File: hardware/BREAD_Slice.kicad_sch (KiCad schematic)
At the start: 23 parts, among them J1 I2C_01x04, J2 Conn_01x10_Female, J3 Screw_Terminal_01x02, J4 Screw_Terminal_01x02, J5 Screw_Terminal_01x02, J6 Screw_Terminal_01x02, U2 ACS723xMATR-10AB, U3 ACS723xMATR-10AB, U4 ACS723xMATR-10AB, U5 ACS723xMATR-10AB

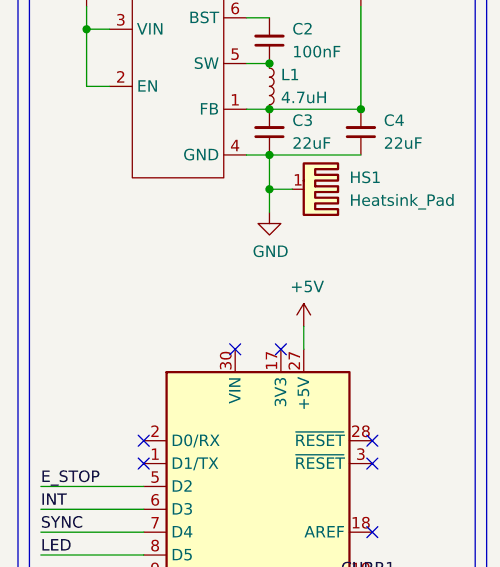
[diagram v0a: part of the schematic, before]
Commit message: updated silkscreen info
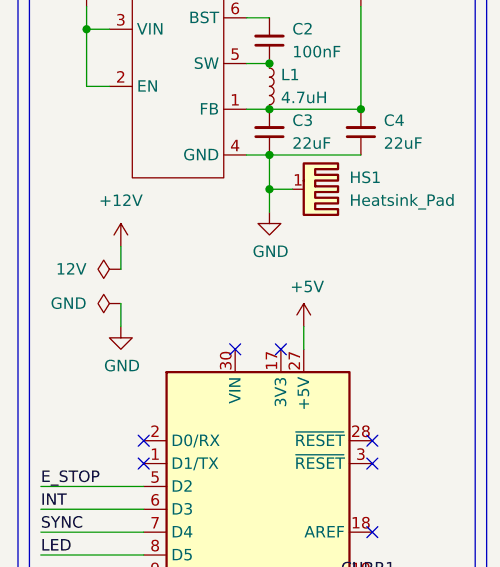
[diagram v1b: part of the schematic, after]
